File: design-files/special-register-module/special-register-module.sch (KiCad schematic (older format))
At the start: 41 parts, among them U402 74HCT377, U403 74HCT161, U404 74HCT161, U405 74HCT245, U406 74HCT245, U407 74HCT377, U408 74HCT245

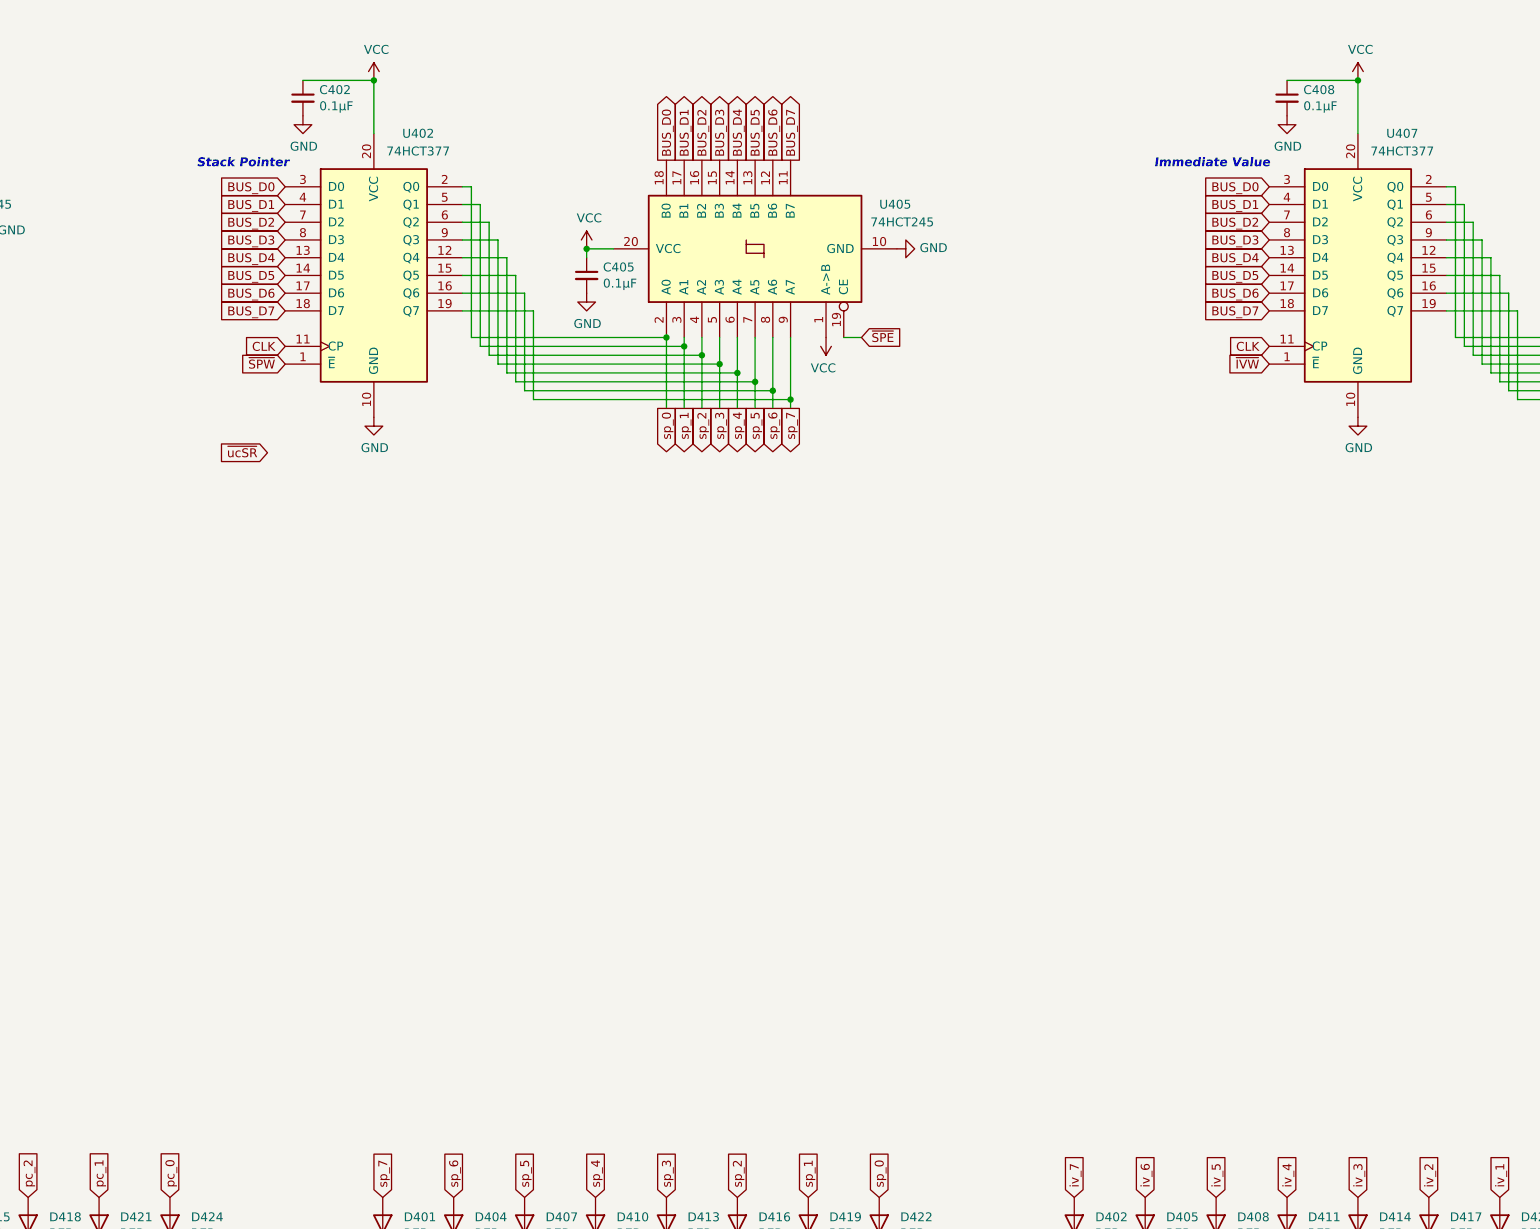
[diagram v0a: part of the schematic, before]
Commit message: Use a pair of 74HCT161s for the stack pointer register; we want the SP to reset to 0 with the ~RST signal.  This saves havint to burn an instruction to initialize the SP at the start of every program.
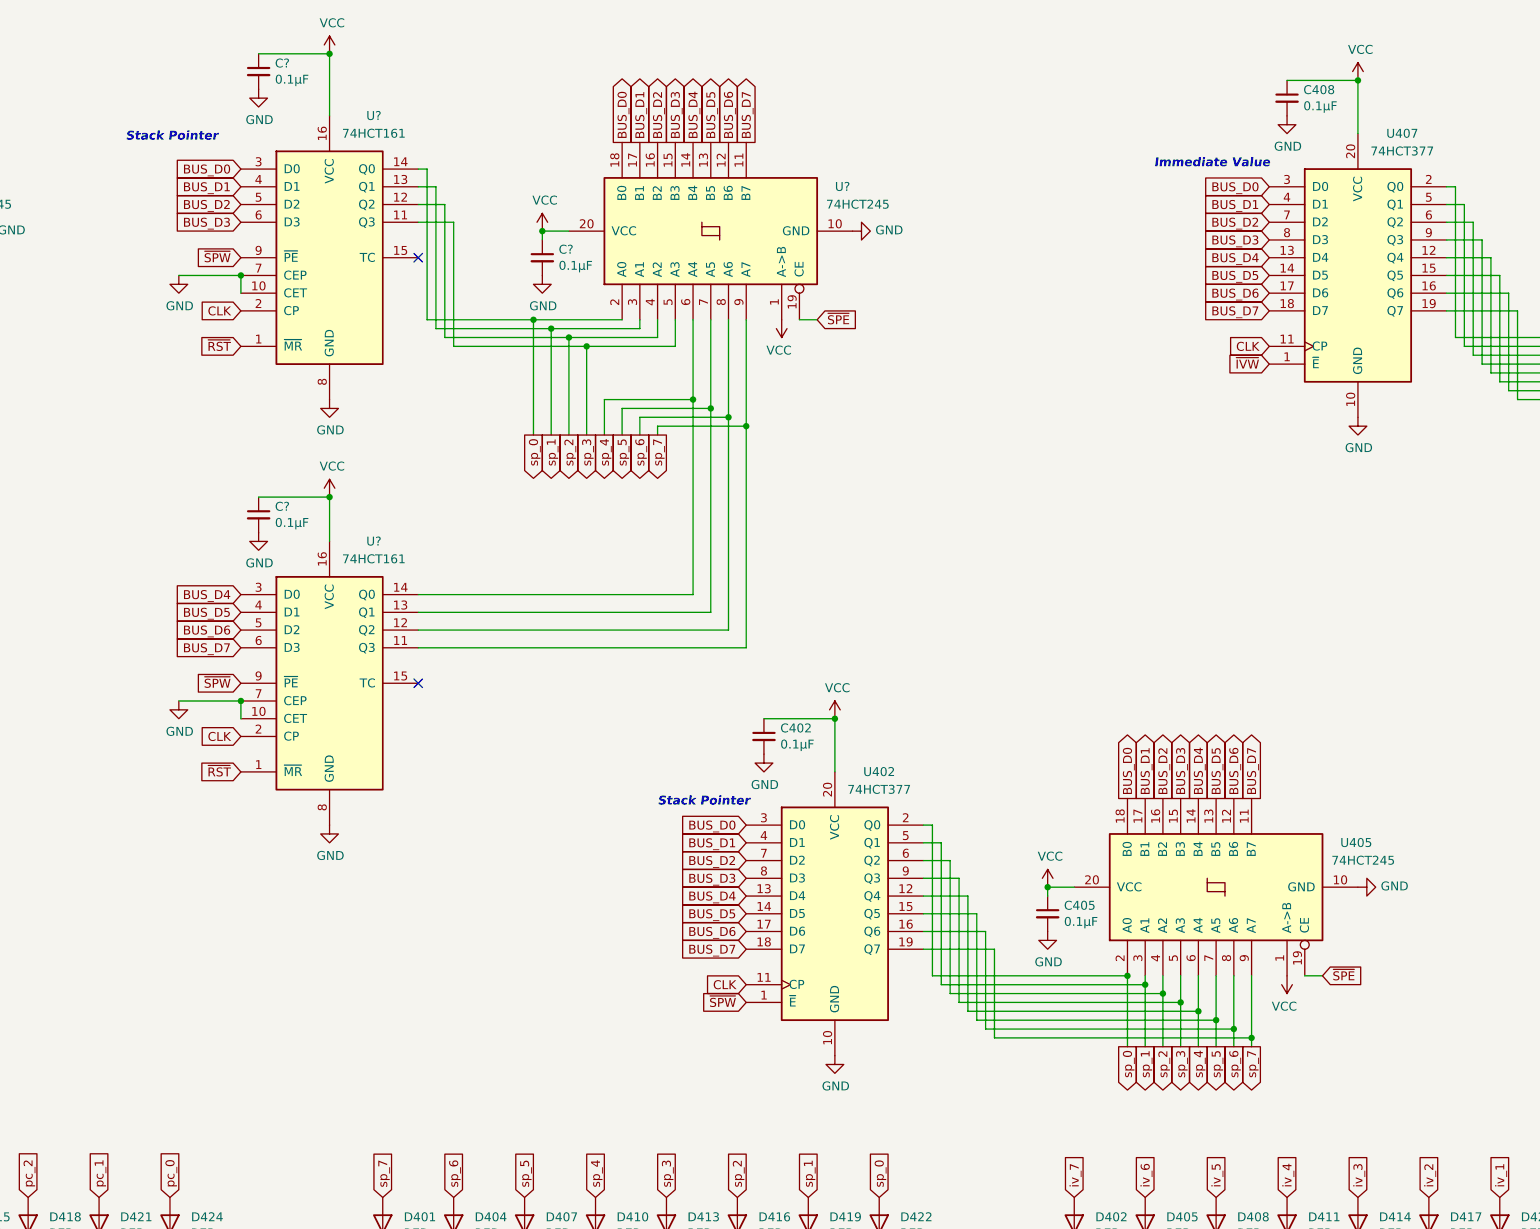
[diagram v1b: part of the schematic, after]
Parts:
- added C? (x3): 0.1µF, Capacitor_THT:C_Radial_D6.3mm_H5.0mm_P2.50mm, symbol Device:C_Small
- added U? (x2): 74HCT161, Package_DIP:DIP-16_W7.62mm_Socket, symbol 74xx:74LS161
- added U?: 74HCT245, Package_DIP:DIP-20_W7.62mm_Socket, symbol 74xx:74LS245
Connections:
- net BUS_D0: now also U?.18 (B0), U?.3 (D0)
- net BUS_D1: now also U?.17 (B1), U?.4 (D1)
- net BUS_D2: now also U?.16 (B2), U?.5 (D2)
- net BUS_D3: now also U?.15 (B3), U?.6 (D3)
- net BUS_D4: now also U?.14 (B4), U?.3 (D0)
- net BUS_D5: now also U?.13 (B5), U?.4 (D1)
- net BUS_D6: now also U?.12 (B6), U?.5 (D2)
- net BUS_D7: now also U?.11 (B7), U?.6 (D3)
- net CLK: now also U?.2 (CP), U?.2 (CP)
- net GND: now also C?.2, C?.2, C?.2, U?.10 (CET), U?.10 (CET), U?.10 (GND), U?.7 (CEP), U?.7 (CEP), U?.8 (GND), U?.8 (GND)
- net VCC: now also C?.1, C?.1, C?.1, U?.1 (A->B), U?.16 (VCC), U?.16 (VCC), U?.20 (VCC)
- net sp_0: now also U?.14 (Q0), U?.2 (A0)
- net sp_1: now also U?.13 (Q1), U?.3 (A1)
- net sp_2: now also U?.12 (Q2), U?.4 (A2)
- net sp_3: now also U?.11 (Q3), U?.5 (A3)
- net sp_4: now also U?.14 (Q0), U?.6 (A4)
- net sp_5: now also U?.13 (Q1), U?.7 (A5)
- net sp_6: now also U?.12 (Q2), U?.8 (A6)
- net sp_7: now also U?.11 (Q3), U?.9 (A7)
- net ~RST: now also U?.1 (~MR), U?.1 (~MR)
- net ~SPE: now also U?.19 (CE)
- net ~SPW: now also U?.9 (~PE), U?.9 (~PE)
- no-connect marks 1 -> 3
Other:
- moved on the sheet: C402, C405, U402, U405

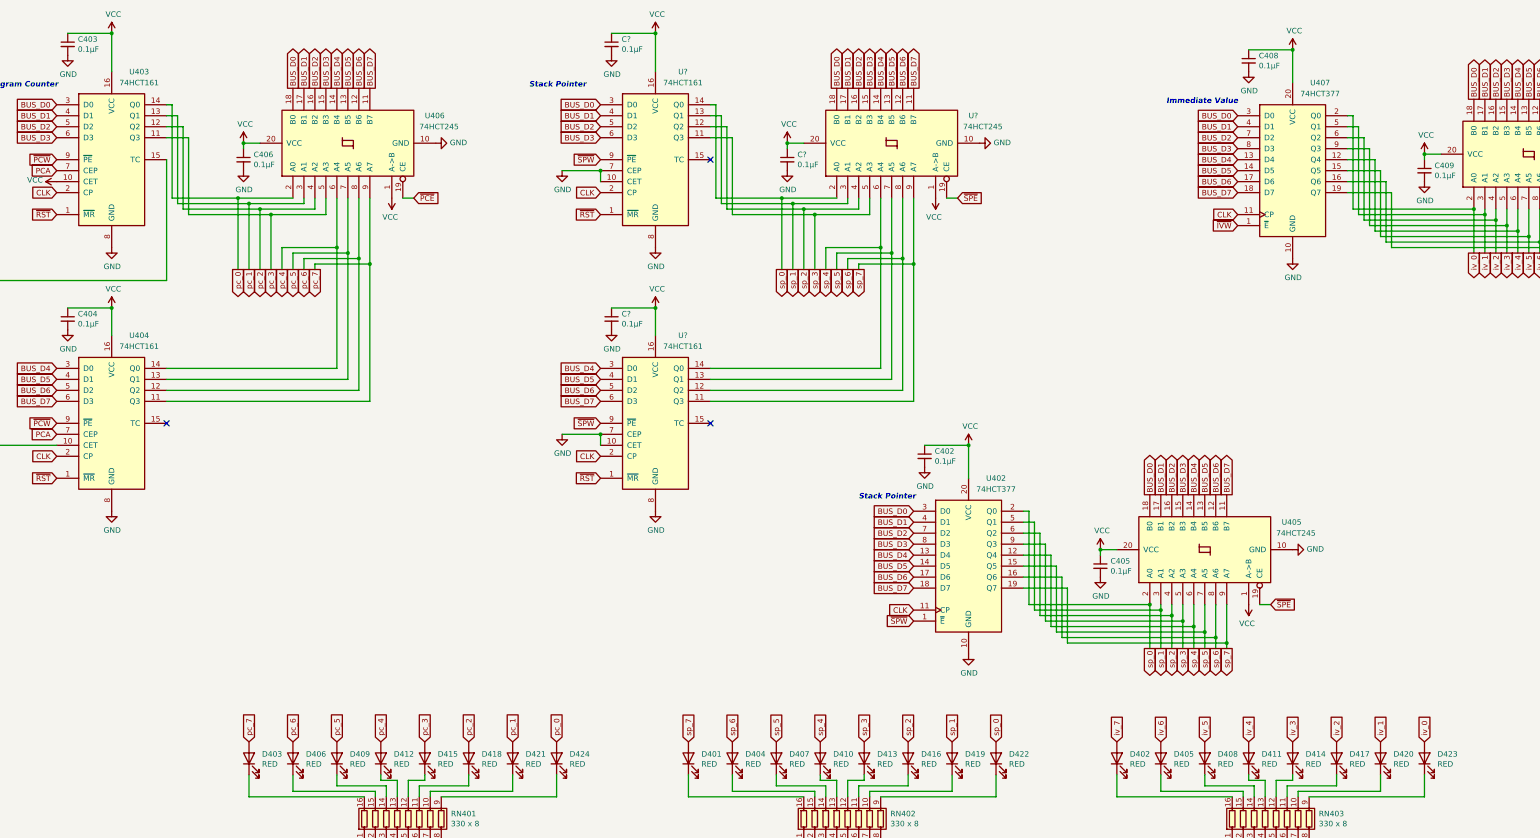
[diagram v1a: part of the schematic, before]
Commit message: Neaten up and re-annotate all of the components in the special register module.
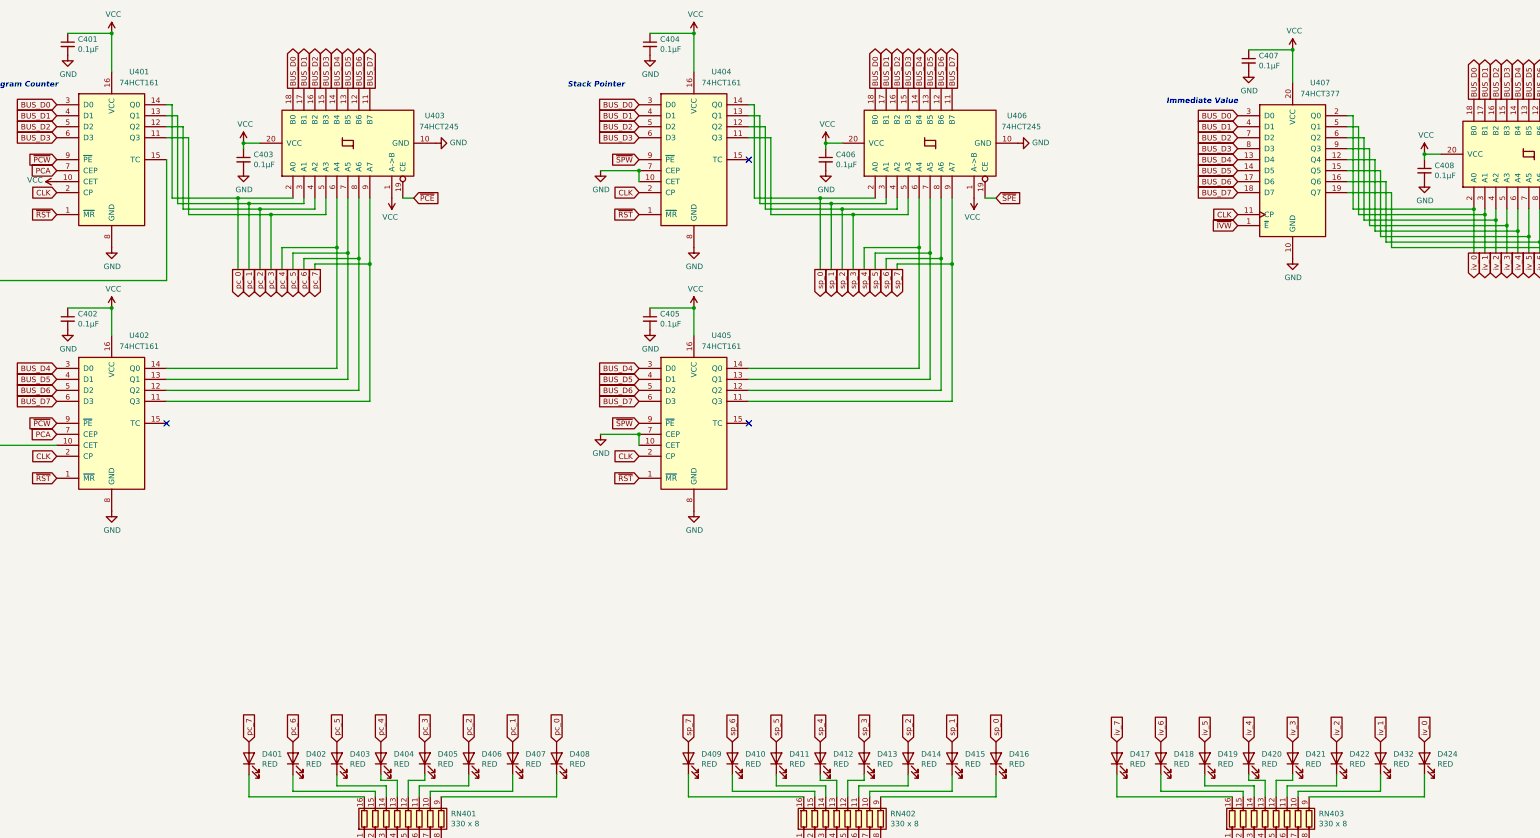
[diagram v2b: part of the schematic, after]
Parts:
- removed C402, C405: 0.1µF, Capacitor_THT:C_Radial_D6.3mm_H5.0mm_P2.50mm, symbol Device:C_Small
- removed U402: 74HCT377, Package_DIP:DIP-20_W7.62mm_Socket, symbol 74xx:74LS377
- removed U405: 74HCT245, Package_DIP:DIP-20_W7.62mm_Socket, symbol 74xx:74LS245
- gave numbers to parts that had none: 6
- renumbered C403 to C401, C404 to C402, C406 to C403, C408 to C407, C409 to C408, D403 to D401, D406 to D402, D409 to D403, D412 to D404, D415 to D405, D418 to D406, D421 to D407, D424 to D408, D401 to D409, D404 to D410, D407 to D411, D410 to D412, D416 to D414, D419 to D415, D422 to D416, D402 to D417, D405 to D418, D408 to D419, D411 to D420, D414 to D421, D417 to D422, D423 to D424, D420 to D432, U403 to U401, U404 to U402, U406 to U403
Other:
- moved on the sheet: C404, C405, C406, U404, U405, U406
